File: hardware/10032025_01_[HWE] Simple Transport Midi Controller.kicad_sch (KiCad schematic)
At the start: 0 parts

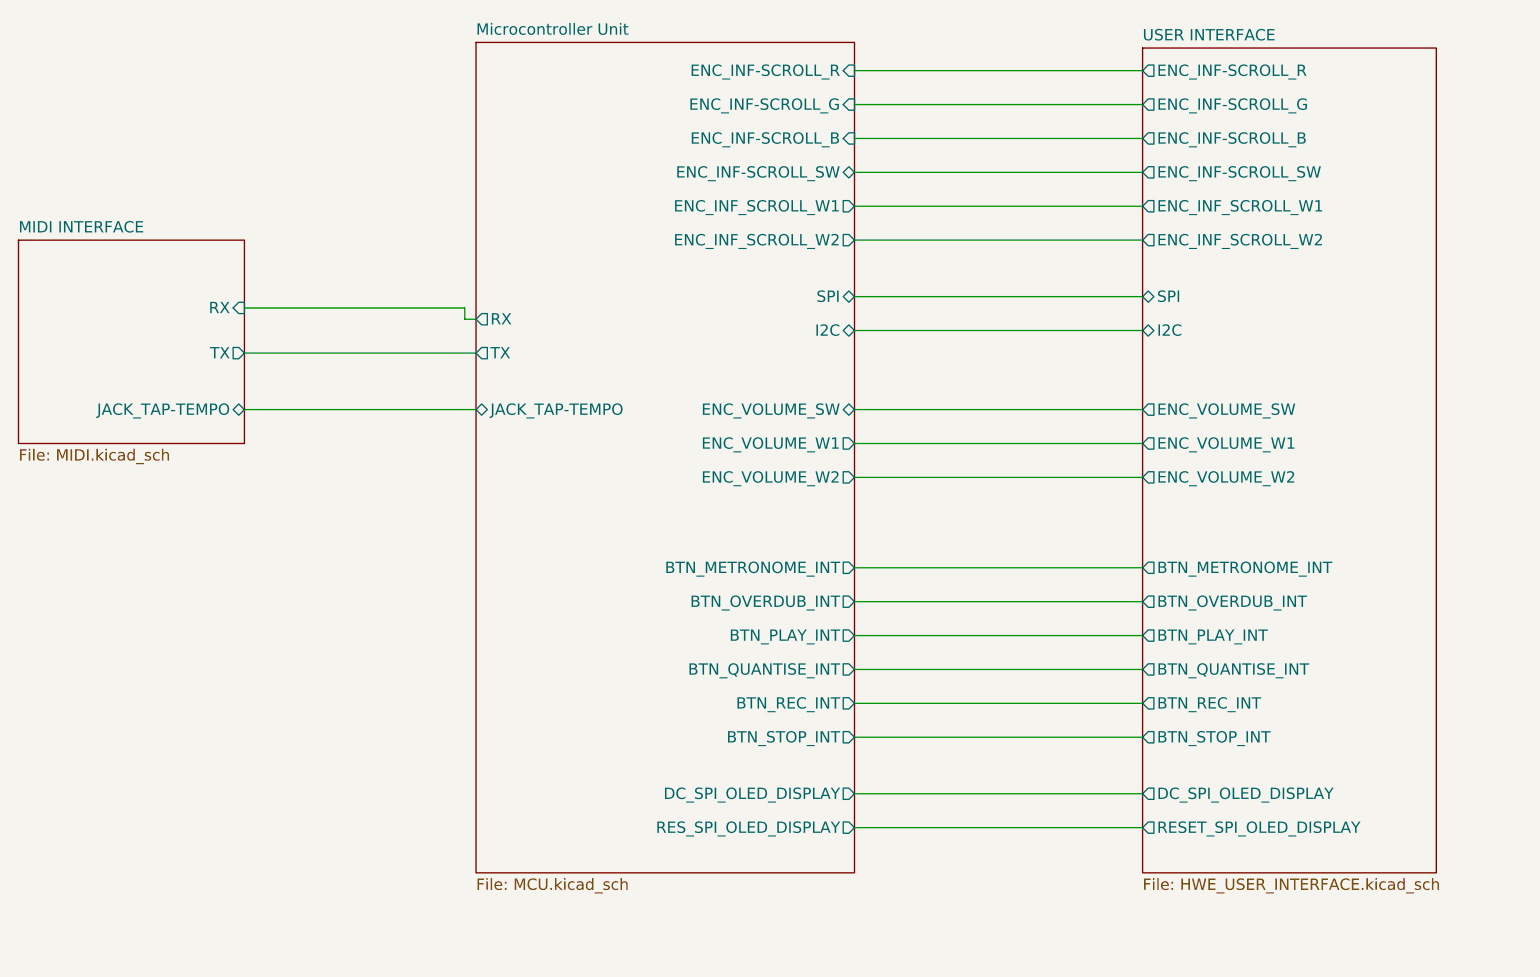
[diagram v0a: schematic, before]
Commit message: feat [HWE]: Attached LED_RING VCC to FET SWITCH
Attached the LED_RING VCC and VIO pins to a FET switch which is driven by the MCU's RESET pin as I was noticing during prototyping a bug that whenever I went into bootloader mode on the ESP32-S3, the system will not send any i2c LED turn off signals to the LED Ring
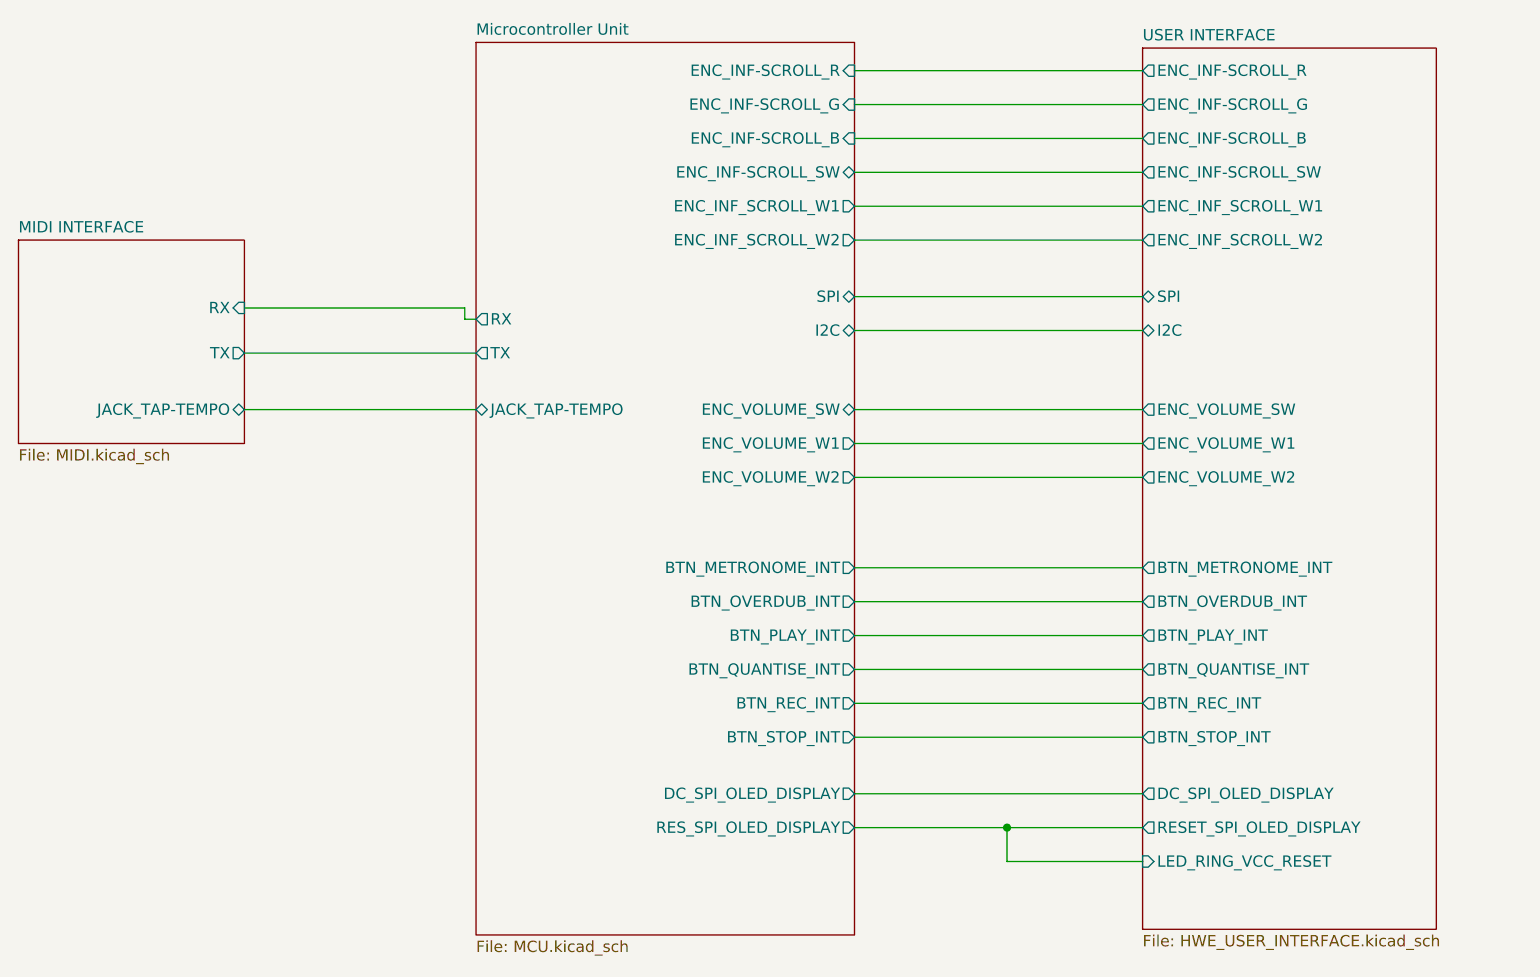
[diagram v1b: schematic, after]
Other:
- sheet USER INTERFACE ports: added LED_RING_VCC_RESET; removed none
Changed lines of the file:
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@@
 		(comment 1 "Used the combination of the Adafruit Feather ESP32-V2 Dev Board and the SX1509 IO expander")
 	)
+	(junction
+		(at 148.59 134.62)
+		(diameter 0)
+		(color 0 0 0 0)
+	)
 	(wire
 		(pts
@@
 	(wire
 		(pts
+			(xy 148.59 134.62) (xy 163.83 134.62)
+		)
+		(stroke
+			(width 0)
+			(type default)
+		)
+	)
+	(wire
+		(pts
+			(xy 148.59 134.62) (xy 148.59 138.43)
+		)
+		(stroke
+			(width 0)
+			(type default)
+		)
+	)
+	(wire
+		(pts
 			(xy 131.445 57.15) (xy 163.83 57.15)
 		)
@@
 	(wire
 		(pts
-			(xy 131.445 134.62) (xy 163.83 134.62)
+			(xy 131.445 134.62) (xy 148.59 134.62)
 		)
 		(stroke
@@
 		(pts
 			(xy 62.865 81.28) (xy 88.9 81.28)
+		)
+		(stroke
+			(width 0)
+			(type default)
+		)
+	)
+	(wire
+		(pts
+			(xy 163.83 138.43) (xy 148.59 138.43)
 		)
 		(stroke
@@
 	(sheet
 		(at 88.9 46.355)
-		(size 42.545 93.345)
+		(size 42.545 100.33)
 		(exclude_from_sim no)
 		(in_bom yes)
@@
 		)
 		(property "Sheetfile" "MCU.kicad_sch"
-			(at 88.9 140.2846 0)
+			(at 88.9 147.2696 0)
 			(effects
 				(font
@@
 	(sheet
 		(at 163.83 46.99)
-		(size 33.02 92.71)
+		(size 33.02 99.06)
 		(exclude_from_sim no)
 		(in_bom yes)
@@
 		)
 		(property "Sheetfile" "HWE_USER_INTERFACE.kicad_sch"
-			(at 163.83 140.2846 0)
+			(at 163.83 146.6346 0)
 			(effects
 				(font
@@
 			(effects
 				(font
+					(size 1.27 1.27)
+				)
+				(justify left)
+			)
+		)
+		(pin "LED_RING_VCC_RESET" input
+			(at 163.83 138.43 180)
+			(effects
+				(font
